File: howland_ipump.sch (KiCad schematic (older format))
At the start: 10 parts, among them U11 OPA991S

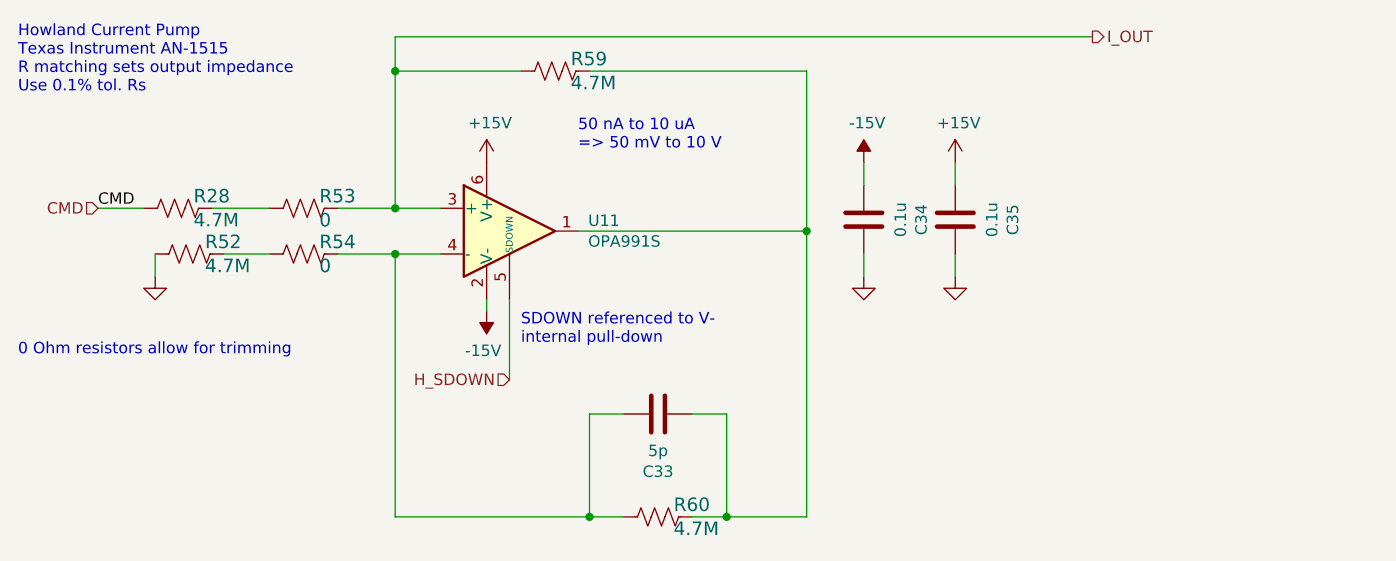
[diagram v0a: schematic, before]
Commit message: removed all references to clamp footprints
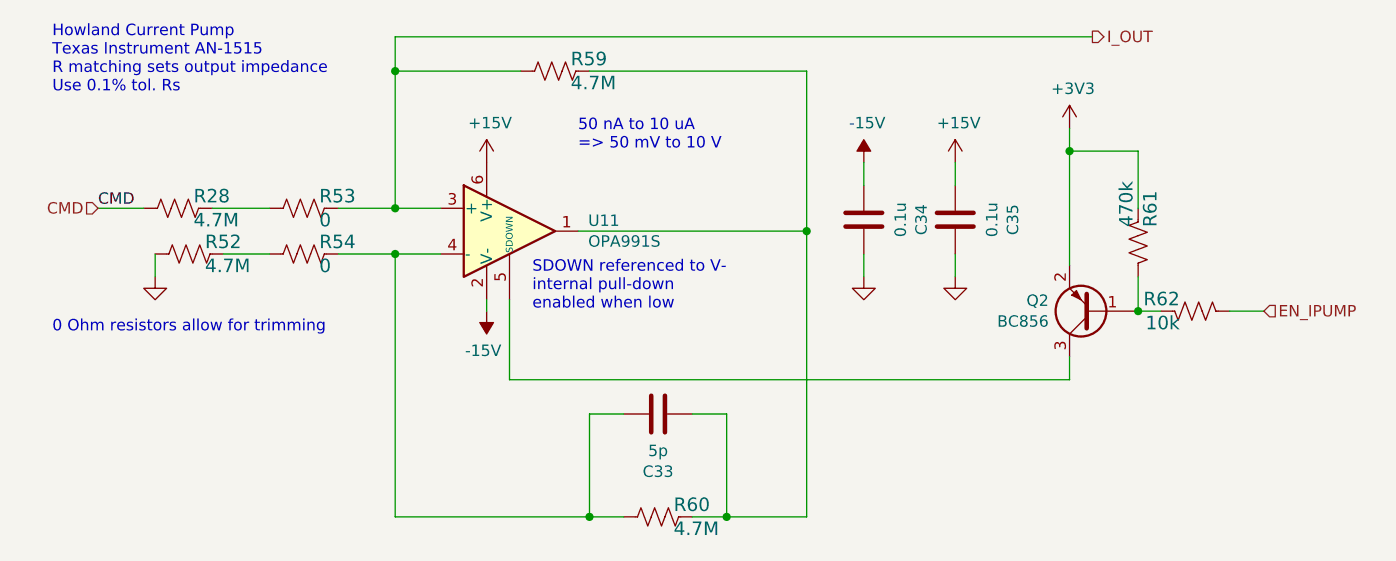
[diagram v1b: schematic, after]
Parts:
- added Q2: BC856, Package_TO_SOT_SMD:SOT-23, symbol Transistor_BJT:BC856
- added R61: 470k, Resistor_SMD:R_0603_1608Metric, symbol Device:R_US
- added R62: 10k, Resistor_SMD:R_0603_1608Metric, symbol Device:R_US
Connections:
- net H_SDOWN: no longer names the net of U11.5 (SDOWN)
- net H_SDOWN: now also Q2.3 (C)
- new net: Q2.1 (B), R61.2, R62.1
- new net +3V3: Q2.2 (E), R61.1
- new net EN_IPUMP: R62.2
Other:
- note added: "SDOWN referenced to V-\ninternal pull-down\nenabled when low\n"
- note removed: "SDOWN referenced to V-\ninternal pull-down\n"
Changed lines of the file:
@@
 AR Path="/6032F251/60D781E3" Ref="#PWR?"  Part="1"
 AR Path="/6032F251/60BDCE3E/60D781E3" Ref="#PWR0146"  Part="1"
+AR Path="/6095BD4C/60BE01FC/60D781E3" Ref="#PWR0116"  Part="1"
+AR Path="/6095BD4C/60C5A41E/60D781E3" Ref="#PWR?"  Part="1"
+AR Path="/61B02572/60BE01FC/60D781E3" Ref="#PWR?"  Part="1"
 F 0 "#PWR0146" H 5100 4150 50  0001 C CNN
 F 1 "-15V" H 5115 4223 50  0000 C CNN
@@
 AR Path="/6032F251/60D781E9" Ref="#PWR?"  Part="1"
 AR Path="/6032F251/60BDCE3E/60D781E9" Ref="#PWR0147"  Part="1"
+AR Path="/6095BD4C/60BE01FC/60D781E9" Ref="#PWR0157"  Part="1"
+AR Path="/6095BD4C/60C5A41E/60D781E9" Ref="#PWR?"  Part="1"
+AR Path="/61B02572/60BE01FC/60D781E9" Ref="#PWR?"  Part="1"
 F 0 "#PWR0147" H 5100 3250 50  0001 C CNN
 F 1 "+15V" H 5115 3573 50  0000 C CNN
@@
 AR Path="/6032F251/60D781F4" Ref="C?"  Part="1"
 AR Path="/6032F251/60BDCE3E/60D781F4" Ref="C33"  Part="1"
+AR Path="/6095BD4C/60BE01FC/60D781F4" Ref="C3"  Part="1"
+AR Path="/6095BD4C/60C5A41E/60D781F4" Ref="C?"  Part="1"
+AR Path="/61B02572/60BE01FC/60D781F4" Ref="C?"  Part="1"
 F 0 "C33" V 5598 4500 50  0000 C CNN
 F 1 "5p" V 5689 4500 50  0000 C CNN
@@
 AR Path="/6032F251/60D78215" Ref="#PWR?"  Part="1"
 AR Path="/6032F251/60BDCE3E/60D78215" Ref="#PWR0148"  Part="1"
+AR Path="/6095BD4C/60BE01FC/60D78215" Ref="#PWR0158"  Part="1"
+AR Path="/6095BD4C/60C5A41E/60D78215" Ref="#PWR?"  Part="1"
+AR Path="/61B02572/60BE01FC/60D78215" Ref="#PWR?"  Part="1"
 F 0 "#PWR0148" H 3650 3650 50  0001 C CNN
 F 1 "GND" V 3655 3772 50  0001 R CNN
@@
 AR Path="/6032F251/60D7821F" Ref="U?"  Part="1"
 AR Path="/6032F251/60BDCE3E/60D7821F" Ref="U11"  Part="1"
+AR Path="/6095BD4C/60BE01FC/60D7821F" Ref="U10"  Part="1"
+AR Path="/6095BD4C/60C5A41E/60D7821F" Ref="U?"  Part="1"
+AR Path="/61B02572/60BE01FC/60D7821F" Ref="U?"  Part="1"
 F 0 "U11" H 5544 3746 50  0000 L CNN
 F 1 "OPA991S" H 5544 3655 50  0000 L CNN
@@
 Wire Wire Line
 	5550 3000 6500 3000
-Text Notes 5250 4200 0    50   ~ 0
-SDOWN referenced to V-\ninternal pull-down\n
-Wire Wire Line
-	5200 4000 5200 4350
+Text Notes 5300 4050 0    50   ~ 0
+SDOWN referenced to V-\ninternal pull-down\nenabled when low\n
 Text Notes 5500 3350 0    50   ~ 0
 50 nA to 10 uA\n=> 50 mV to 10 V
@@
 AR Path="/6032F251/60D78240" Ref="R?"  Part="1"
 AR Path="/6032F251/60BDCE3E/60D78240" Ref="R60"  Part="1"
+AR Path="/6095BD4C/60BE01FC/60D78240" Ref="R19"  Part="1"
+AR Path="/6095BD4C/60C5A41E/60D78240" Ref="R?"  Part="1"
+AR Path="/61B02572/60BE01FC/60D78240" Ref="R?"  Part="1"
 F 0 "R60" V 5797 5018 59  0000 L CNN
 F 1 "4.7M" V 5902 5018 59  0000 L CNN
@@
 	0    1    1    0
 $EndComp
-Text Notes 3050 3100 0    50   ~ 0
+Text Notes 3200 3100 0    50   ~ 0
 Howland Current Pump\nTexas Instrument AN-1515\nR matching sets output impedance\nUse 0.1% tol. Rs
 $Comp
@@
 AR Path="/6032F251/608FDC40/60D7824A" Ref="C?"  Part="1"
 AR Path="/6032F251/60BDCE3E/60D7824A" Ref="C34"  Part="1"
+AR Path="/6095BD4C/60BE01FC/60D7824A" Ref="C4"  Part="1"
+AR Path="/6095BD4C/60C5A41E/60D7824A" Ref="C?"  Part="1"
+AR Path="/61B02572/60BE01FC/60D7824A" Ref="C?"  Part="1"
 F 0 "C34" V 6498 3650 50  0000 C CNN
 F 1 "0.1u" V 6589 3650 50  0000 C CNN
@@
 AR Path="/6032F251/608FDC40/60D78250" Ref="#PWR?"  Part="1"
 AR Path="/6032F251/60BDCE3E/60D78250" Ref="#PWR0157"  Part="1"
+AR Path="/6095BD4C/60BE01FC/60D78250" Ref="#PWR0163"  Part="1"
+AR Path="/6095BD4C/60C5A41E/60D78250" Ref="#PWR?"  Part="1"
+AR Path="/61B02572/60BE01FC/60D78250" Ref="#PWR?"  Part="1"
 F 0 "#PWR0157" H 6750 3650 50  0001 C CNN
 F 1 "GND" V 6755 3772 50  0001 R CNN
@@
 AR Path="/6032F251/608FDC40/60D78256" Ref="#PWR?"  Part="1"
 AR Path="/6032F251/60BDCE3E/60D78256" Ref="#PWR0158"  Part="1"
+AR Path="/6095BD4C/60BE01FC/60D78256" Ref="#PWR0164"  Part="1"
+AR Path="/6095BD4C/60C5A41E/60D78256" Ref="#PWR?"  Part="1"
+AR Path="/61B02572/60BE01FC/60D78256" Ref="#PWR?"  Part="1"
 F 0 "#PWR0158" H 7150 3250 50  0001 C CNN
 F 1 "+15V" H 7165 3573 50  0000 C CNN
@@
 AR Path="/6032F251/608FDC40/60D7825C" Ref="#PWR?"  Part="1"
 AR Path="/6032F251/60BDCE3E/60D7825C" Ref="#PWR0159"  Part="1"
+AR Path="/6095BD4C/60BE01FC/60D7825C" Ref="#PWR0165"  Part="1"
+AR Path="/6095BD4C/60C5A41E/60D7825C" Ref="#PWR?"  Part="1"
+AR Path="/61B02572/60BE01FC/60D7825C" Ref="#PWR?"  Part="1"
 F 0 "#PWR0159" H 7150 3650 50  0001 C CNN
 F 1 "GND" V 7155 3772 50  0001 R CNN
@@
 AR Path="/6032F251/608FDC40/60D78264" Ref="C?"  Part="1"
 AR Path="/6032F251/60BDCE3E/60D78264" Ref="C35"  Part="1"
+AR Path="/6095BD4C/60BE01FC/60D78264" Ref="C5"  Part="1"
+AR Path="/6095BD4C/60C5A41E/60D78264" Ref="C?"  Part="1"
+AR Path="/61B02572/60BE01FC/60D78264" Ref="C?"  Part="1"
 F 0 "C35" V 6898 3650 50  0000 C CNN
 F 1 "0.1u" V 6989 3650 50  0000 C CNN
@@
 AR Path="/6032F251/608FDC40/60D7826A" Ref="#PWR?"  Part="1"
 AR Path="/6032F251/60BDCE3E/60D7826A" Ref="#PWR0160"  Part="1"
+AR Path="/6095BD4C/60BE01FC/60D7826A" Ref="#PWR0166"  Part="1"
+AR Path="/6095BD4C/60C5A41E/60D7826A" Ref="#PWR?"  Part="1"
+AR Path="/61B02572/60BE01FC/60D7826A" Ref="#PWR?"  Part="1"
 F 0 "#PWR0160" H 6750 3500 50  0001 C CNN
 F 1 "-15V" H 6765 3573 50  0000 C CNN
@@
 Text HLabel 3400 3600 0    50   Input ~ 0
 CMD
-Text HLabel 5200 4350 0    50   Input ~ 0
-H_SDOWN
 Wire Wire Line
 	5550 4500 5700 4500
@@
 AR Path="/6032F251/60D83006" Ref="R?"  Part="1"
 AR Path="/6032F251/60BDCE3E/60D83006" Ref="R54"  Part="1"
+AR Path="/6095BD4C/60BE01FC/60D83006" Ref="R17"  Part="1"
+AR Path="/6095BD4C/60C5A41E/60D83006" Ref="R?"  Part="1"
+AR Path="/61B02572/60BE01FC/60D83006" Ref="R?"  Part="1"
 F 0 "R54" V 4247 3868 59  0000 L CNN
 F 1 "0" V 4352 3868 59  0000 L CNN
@@
 AR Path="/6032F251/60D8879F" Ref="R?"  Part="1"
 AR Path="/6032F251/60BDCE3E/60D8879F" Ref="R53"  Part="1"
+AR Path="/6095BD4C/60BE01FC/60D8879F" Ref="R16"  Part="1"
+AR Path="/6095BD4C/60C5A41E/60D8879F" Ref="R?"  Part="1"
+AR Path="/61B02572/60BE01FC/60D8879F" Ref="R?"  Part="1"
 F 0 "R53" V 4247 3668 59  0000 L CNN
 F 1 "0" V 4352 3668 59  0000 L CNN
@@
 	4450 3600 4700 3600
 Connection ~ 4700 3600
-Text Notes 3050 4250 0    50   ~ 0
+Text Notes 3200 4150 0    50   ~ 0
 0 Ohm resistors allow for trimming
 $Comp
@@
 AR Path="/6032F251/60B385AE" Ref="R?"  Part="1"
 AR Path="/6032F251/60BDCE3E/60B385AE" Ref="R52"  Part="1"
+AR Path="/6095BD4C/60BE01FC/60B385AE" Ref="R15"  Part="1"
+AR Path="/6095BD4C/60C5A41E/60B385AE" Ref="R?"  Part="1"
+AR Path="/61B02572/60BE01FC/60B385AE" Ref="R?"  Part="1"
 F 0 "R52" V 3747 3868 59  0000 L CNN
 F 1 "4.7M" V 3852 3868 59  0000 L CNN
@@
 AR Path="/6032F251/60B38EA4" Ref="R?"  Part="1"
 AR Path="/6032F251/60BDCE3E/60B38EA4" Ref="R28"  Part="1"
+AR Path="/6095BD4C/60BE01FC/60B38EA4" Ref="R14"  Part="1"
+AR Path="/6095BD4C/60C5A41E/60B38EA4" Ref="R?"  Part="1"
+AR Path="/61B02572/60BE01FC/60B38EA4" Ref="R?"  Part="1"
 F 0 "R28" V 3697 3668 59  0000 L CNN
 F 1 "4.7M" V 3802 3668 59  0000 L CNN
@@
 AR Path="/6032F251/60B3940D" Ref="R?"  Part="1"
 AR Path="/6032F251/60BDCE3E/60B3940D" Ref="R59"  Part="1"
+AR Path="/6095BD4C/60BE01FC/60B3940D" Ref="R18"  Part="1"
+AR Path="/6095BD4C/60C5A41E/60B3940D" Ref="R?"  Part="1"
+AR Path="/61B02572/60BE01FC/60B3940D" Ref="R?"  Part="1"
 F 0 "R59" V 5347 3068 59  0000 L CNN
 F 1 "4.7M" V 5452 3068 59  0000 L CNN
@@
 	0    1    1    0
 $EndComp
+$Comp
+L Transistor_BJT:BC856 Q2
+U 1 1 60BEDC00
+P 7750 4050
+F 0 "Q2" H 7941 4004 50  0000 L CNN
+F 1 "BC856" H 7941 4095 50  0000 L CNN
+F 2 "Package_TO_SOT_SMD:SOT-23" H 7950 3975 50  0001 L CIN
+F 3 "https://www.onsemi.com/pub/Collateral/BC860-D.pdf" H 7750 4050 50  0001 L CNN
+	1    7750 4050
+	-1   0    0    1
+$EndComp
+$Comp
+L Device:R_US R?
+U 1 1 60BF0E09
+P 8200 4050
+AR Path="/6032F251/60BF0E09" Ref="R?"  Part="1"
+AR Path="/6032F251/60BDCE3E/60BF0E09" Ref="R62"  Part="1"
+AR Path="/6095BD4C/60BE01FC/60BF0E09" Ref="R?"  Part="1"
+AR Path="/6095BD4C/60C5A41E/60BF0E09" Ref="R?"  Part="1"
+AR Path="/61B02572/60BE01FC/60BF0E09" Ref="R?"  Part="1"
+F 0 "R62" V 8147 4118 59  0000 L CNN
+F 1 "10k" V 8252 4118 59  0000 L CNN
+F 2 "Resistor_SMD:R_0603_1608Metric" H 8200 4050 50  0001 C CNN
+F 3 "" H 8200 4050 50  0001 C CNN
+F 4 "RC0603FR-0710KL" H 8147 4218 50  0001 C CNN "Manf#"
+F 5 "0.1" H 8200 4050 50  0001 C CNN "Tolerance"
+	1    8200 4050
+	0    -1   1    0
+$EndComp
+$Comp
+L power:+3V3 #PWR0170
+U 1 1 60BF2F91
+P 7650 3250
+F 0 "#PWR0170" H 7650 3100 50  0001 C CNN
+F 1 "+3V3" H 7665 3423 50  0000 C CNN
+F 2 "" H 7650 3250 50  0001 C CNN
+F 3 "" H 7650 3250 50  0001 C CNN
+	1    7650 3250
+	1    0    0    -1
+$EndComp
+Wire Wire Line
+	7950 4050 8050 4050
+Wire Wire Line
+	8350 4050 8500 4050
+Wire Wire Line
+	5200 4000 5200 4350
+Wire Wire Line
+	5200 4350 7650 4350
+Wire Wire Line
+	7650 4350 7650 4250
+Text HLabel 8500 4050 2    50   Input ~ 0
+EN_IPUMP
+Wire Wire Line
+	7650 3250 7650 3350
+$Comp
+L Device:R_US R?
+U 1 1 60C16A39
+P 7950 3750
+AR Path="/6032F251/60C16A39" Ref="R?"  Part="1"
+AR Path="/6032F251/60BDCE3E/60C16A39" Ref="R61"  Part="1"
+AR Path="/6095BD4C/60BE01FC/60C16A39" Ref="R?"  Part="1"
+AR Path="/6095BD4C/60C5A41E/60C16A39" Ref="R?"  Part="1"
+AR Path="/61B02572/60BE01FC/60C16A39" Ref="R?"  Part="1"
+F 0 "R61" V 7897 3818 59  0000 L CNN
+F 1 "470k" V 8002 3818 59  0000 L CNN
+F 2 "Resistor_SMD:R_0603_1608Metric" H 7950 3750 50  0001 C CNN
+F 3 "" H 7950 3750 50  0001 C CNN
+F 4 "RC0603FR-0710KL" H 7897 3918 50  0001 C CNN "Manf#"
+F 5 "0.1" H 7950 3750 50  0001 C CNN "Tolerance"
+	1    7950 3750
+	-1   0    0    -1
+$EndComp
+Wire Wire Line
+	7950 4050 7950 3900
+Connection ~ 7950 4050
+Wire Wire Line
+	7650 3350 7950 3350
+Wire Wire Line
+	7950 3350 7950 3600
+Connection ~ 7650 3350
+Wire Wire Line
+	7650 3350 7650 3850
 $EndSCHEMATC

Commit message: layout updates; part positioning
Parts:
- Q2: Manf# (none) -> BC856B-7-F
- U11: Manf# (none) -> OPA991SIDBVR
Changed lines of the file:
@@
 F 2 "Package_TO_SOT_SMD:SOT-23-6" H 5350 3450 50  0001 L CNN
 F 3 "https://www.ti.com/lit/ds/symlink/opa991.pdf" H 5350 3850 50  0001 C CNN
+F 4 "OPA991SIDBVR" H 5200 3700 50  0001 C CNN "Manf#"
 	1    5200 3700
 	1    0    0    -1
@@
 F 2 "Package_TO_SOT_SMD:SOT-23" H 7950 3975 50  0001 L CIN
 F 3 "https://www.onsemi.com/pub/Collateral/BC860-D.pdf" H 7750 4050 50  0001 L CNN
+F 4 "BC856B-7-F" H 7750 4050 50  0001 C CNN "Manf#"
 	1    7750 4050
 	-1   0    0    1

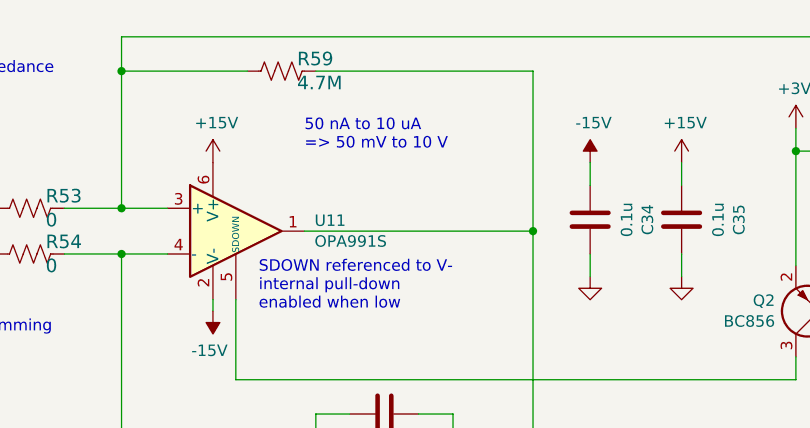
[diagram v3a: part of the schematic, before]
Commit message: updates to README
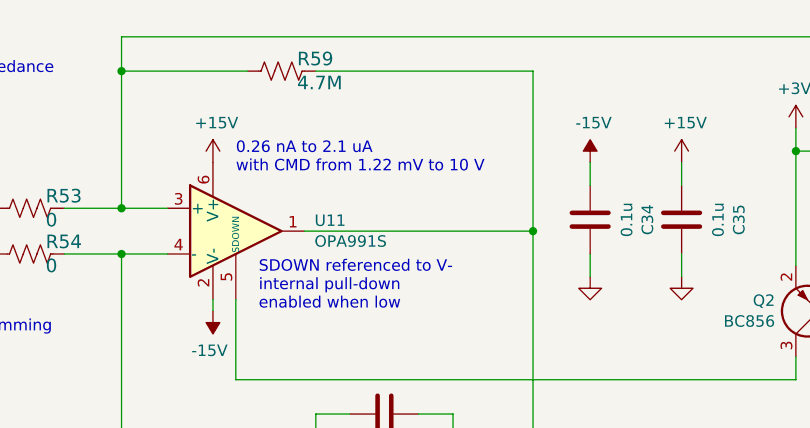
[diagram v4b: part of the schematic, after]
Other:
- note added: "0.26 nA to 2.1 uA\nwith CMD from 1.22 mV to 10 V"
- note removed: "50 nA to 10 uA\n=> 50 mV to 10 V"
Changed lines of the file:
@@
 Text Notes 5300 4050 0    50   ~ 0
 SDOWN referenced to V-\ninternal pull-down\nenabled when low\n
-Text Notes 5500 3350 0    50   ~ 0
-50 nA to 10 uA\n=> 50 mV to 10 V
+Text Notes 5200 3450 0    50   ~ 0
+0.26 nA to 2.1 uA\nwith CMD from 1.22 mV to 10 V
 $Comp
 L Device:R_US R?

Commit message: updating git so that kicad schematic matches pdf doc
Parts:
- R61: Manf# RC0603FR-0710KL -> RC0603FR-07470KL
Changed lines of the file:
@@
 F 2 "Resistor_SMD:R_0603_1608Metric" H 7950 3750 50  0001 C CNN
 F 3 "" H 7950 3750 50  0001 C CNN
-F 4 "RC0603FR-0710KL" H 7897 3918 50  0001 C CNN "Manf#"
+F 4 "RC0603FR-07470KL" H 7897 3918 50  0001 C CNN "Manf#"
 F 5 "0.1" H 7950 3750 50  0001 C CNN "Tolerance"
 	1    7950 3750

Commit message: updates to schematic for alternate part #s
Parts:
- U11: Alternate Manf# (none) -> OPA990SIDBVR
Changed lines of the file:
@@
 F 3 "https://www.ti.com/lit/ds/symlink/opa991.pdf" H 5350 3850 50  0001 C CNN
 F 4 "OPA991SIDBVR" H 5200 3700 50  0001 C CNN "Manf#"
+F 5 "OPA990SIDBVR" H 5200 3700 50  0001 C CNN "Alternate Manf#"
 	1    5200 3700
 	1    0    0    -1
